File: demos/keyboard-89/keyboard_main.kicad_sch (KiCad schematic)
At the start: 7 parts, among them J2 SWD, U1 RP2040, Y1 12MHz

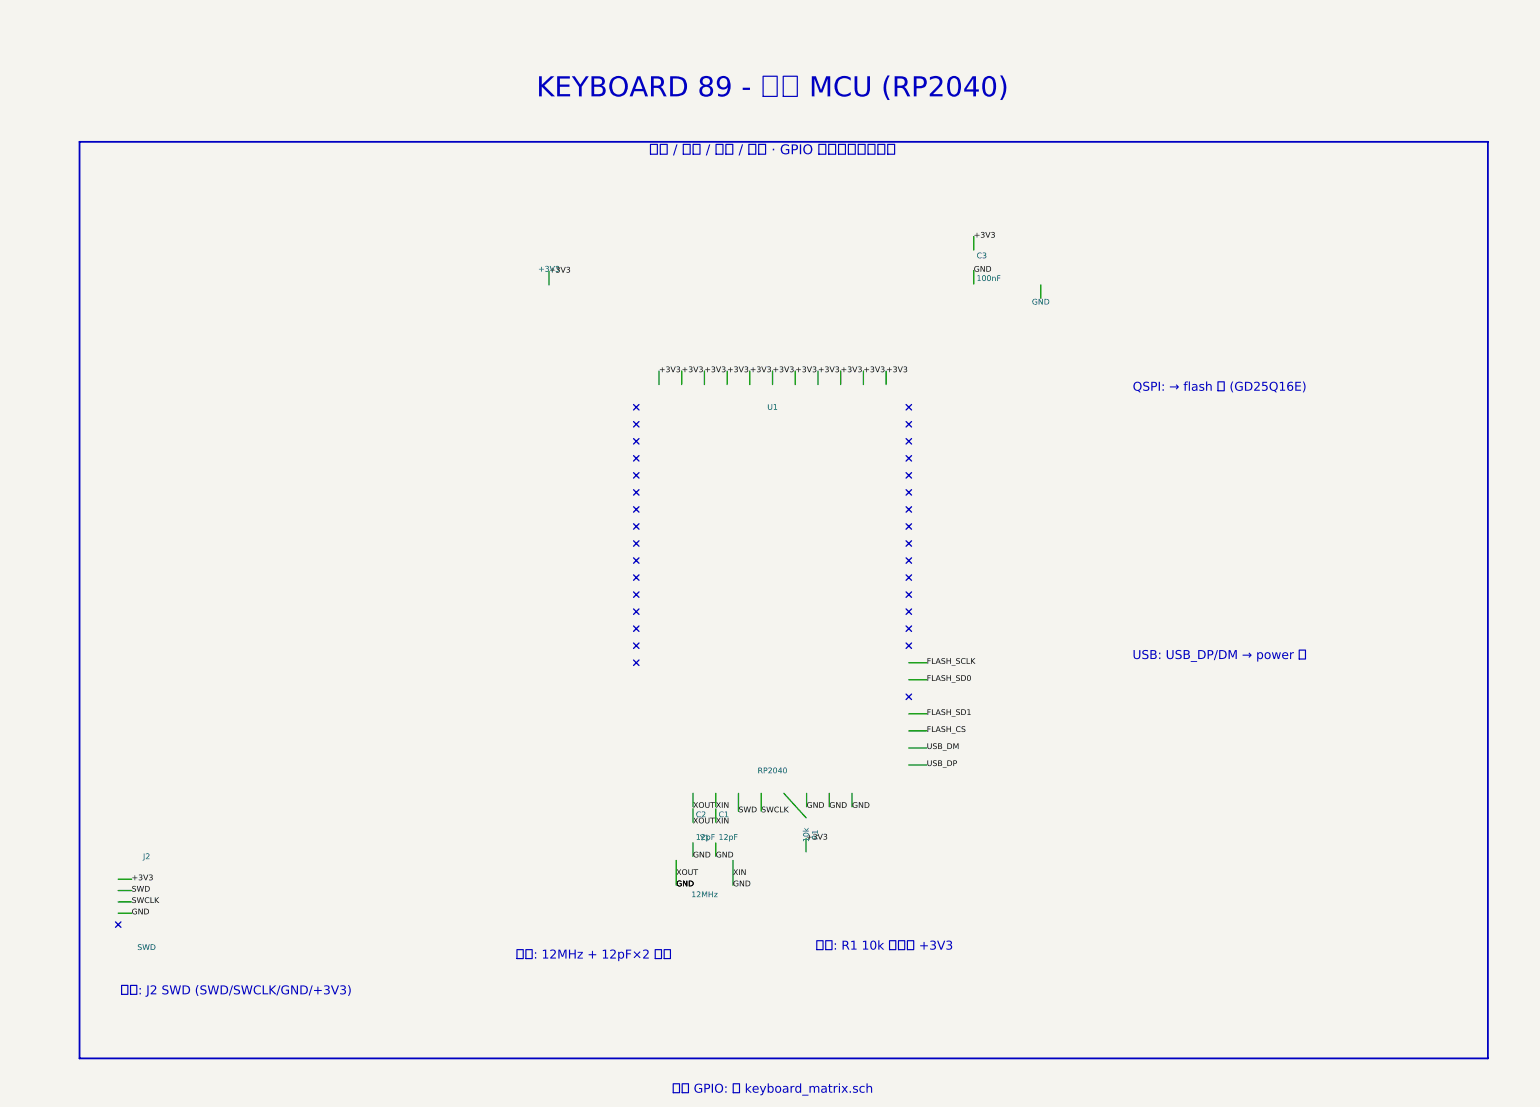
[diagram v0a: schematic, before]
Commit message: fix: update default label height in kicad_sch_add_label function to 1.27mm
feat: add redraw_kb89.py script for redrawing keyboard-89 schematic with new tools
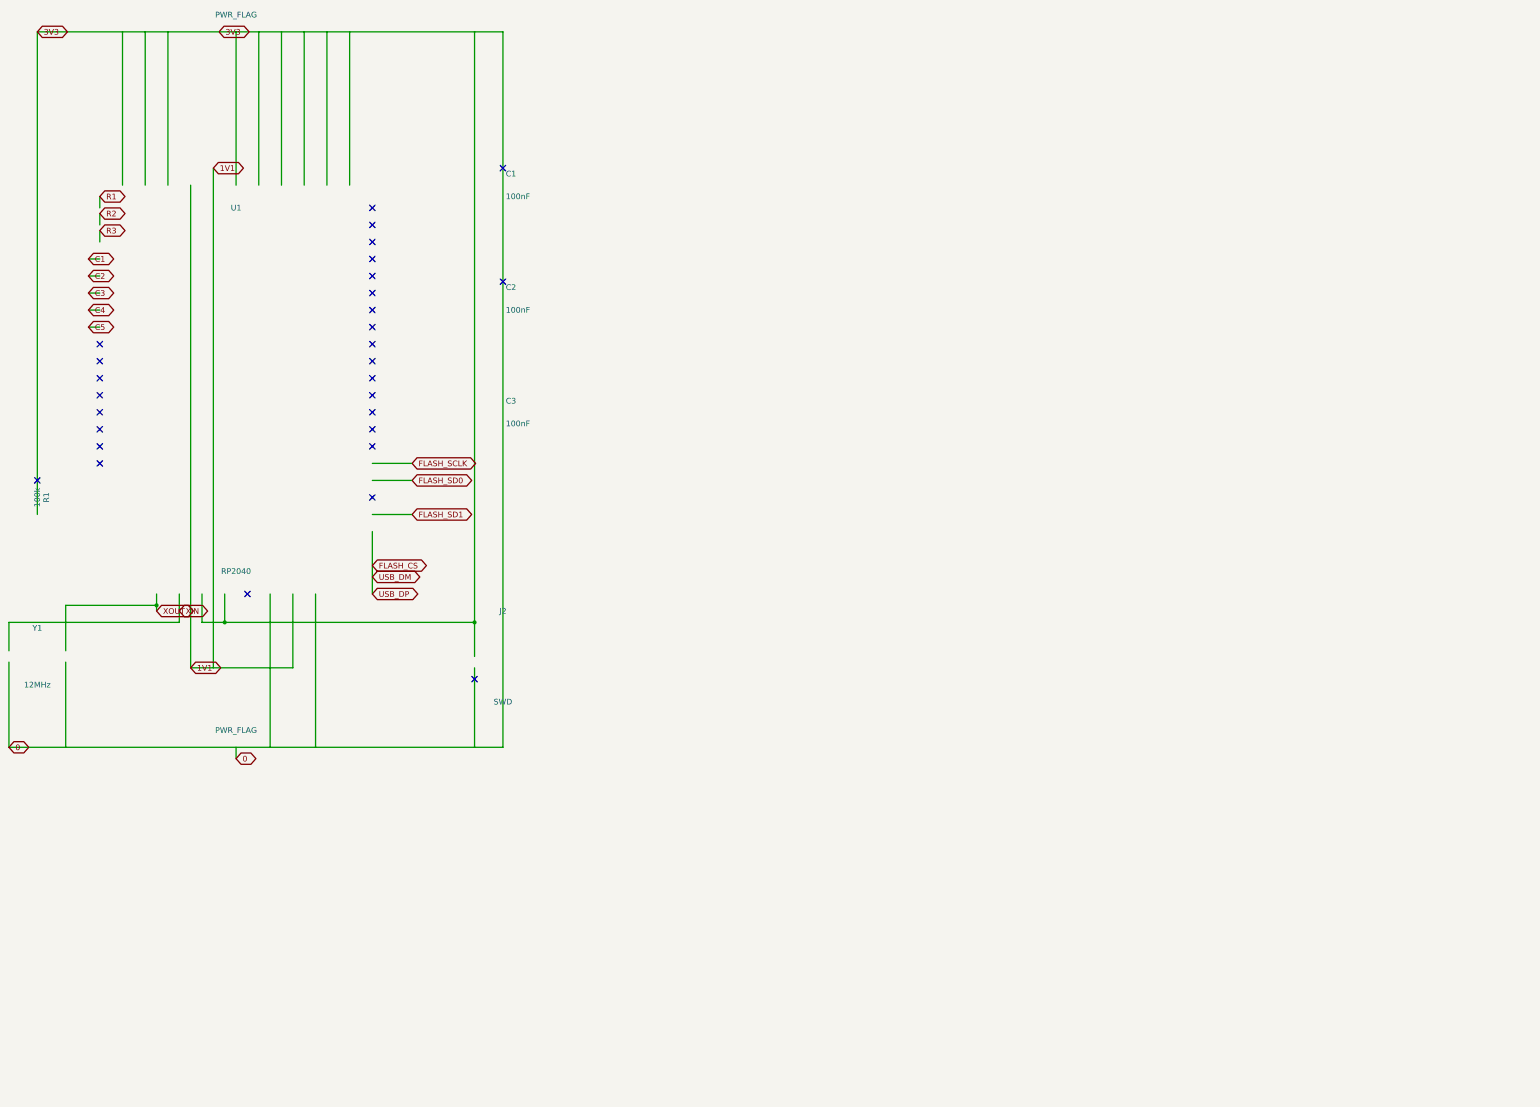
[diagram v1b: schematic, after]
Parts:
- C1, C2: value 12pF -> 100nF
- R1: value 10k -> 100k
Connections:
- net USB_DP is gone; now on net FLASH_CS: U1.47 (USB_DP)
- net at R1.1: no longer U1.26 (RUN)
- net 0: now reaches Y1.4 (GND)
- net 0: now also R1.2
- net R1: now reaches U1.2 (GPIO0)
- net R2: now reaches U1.3 (GPIO1)
- net R3: now reaches U1.4 (GPIO2)
- net C1: now reaches U1.5 (GPIO3)
- net C2: now reaches U1.6 (GPIO4)
- net C3: now reaches U1.7 (GPIO5)
- net C4: now reaches U1.8 (GPIO6)
- net C5: now reaches U1.9 (GPIO7)
- removed net +3V3: C3.1, J2.1, R1.2, U1.1 (IOVDD), U1.10 (IOVDD), U1.22 (IOVDD), U1.23 (DVDD), U1.33 (IOVDD), U1.42 (IOVDD), U1.43 (ADC_AVDD), U1.44 (VREG_VIN), U1.48 (USB_VDD), U1.49 (IOVDD), U1.50 (DVDD)
- removed net GND: C1.1, C1.2, C2.1, C2.2, C3.2, J2.4, U1.19 (TESTEN), U1.20 (XIN), U1.21 (XOUT), U1.45 (VREG_VOUT), U1.57 (GND), Y1.1 (OSC1), Y1.3 (OSC2)
- net SWCLK: no longer names the net of J2.3, U1.24 (SWCLK)
- net SWCLK: now also U1.25 (SWD)
- net SWD: no longer names the net of J2.2
- net SWD: no longer U1.25 (SWD)
- net USB_DM: no longer names the net of U1.46 (USB_DM)
- new net 1V1: U1.45 (VREG_VOUT), U1.50 (DVDD)
- new net XIN: U1.20 (XIN), Y1.1 (OSC1)
- new net XOUT: U1.21 (XOUT), Y1.3 (OSC2)
- no-connect marks 33 -> 29
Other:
- note removed: "KEYBOARD 89 - 主控 MCU (RP2040)"
- note removed: "QSPI: → flash 页 (GD25Q16E)"
- note removed: "USB: USB_DP/DM → power 页"
- note removed: "复位: R1 10k 上拉至 +3V3"
- note removed: "时钟 / 电源 / 复位 / 调试 · GPIO 与矩阵连接见各页"
- note removed: "时钟: 12MHz + 12pF×2 负载"
- note removed: "矩阵 GPIO: 见 keyboard_matrix.sch"
- note removed: "调试: J2 SWD (SWD/SWCLK/GND/+3V3)"

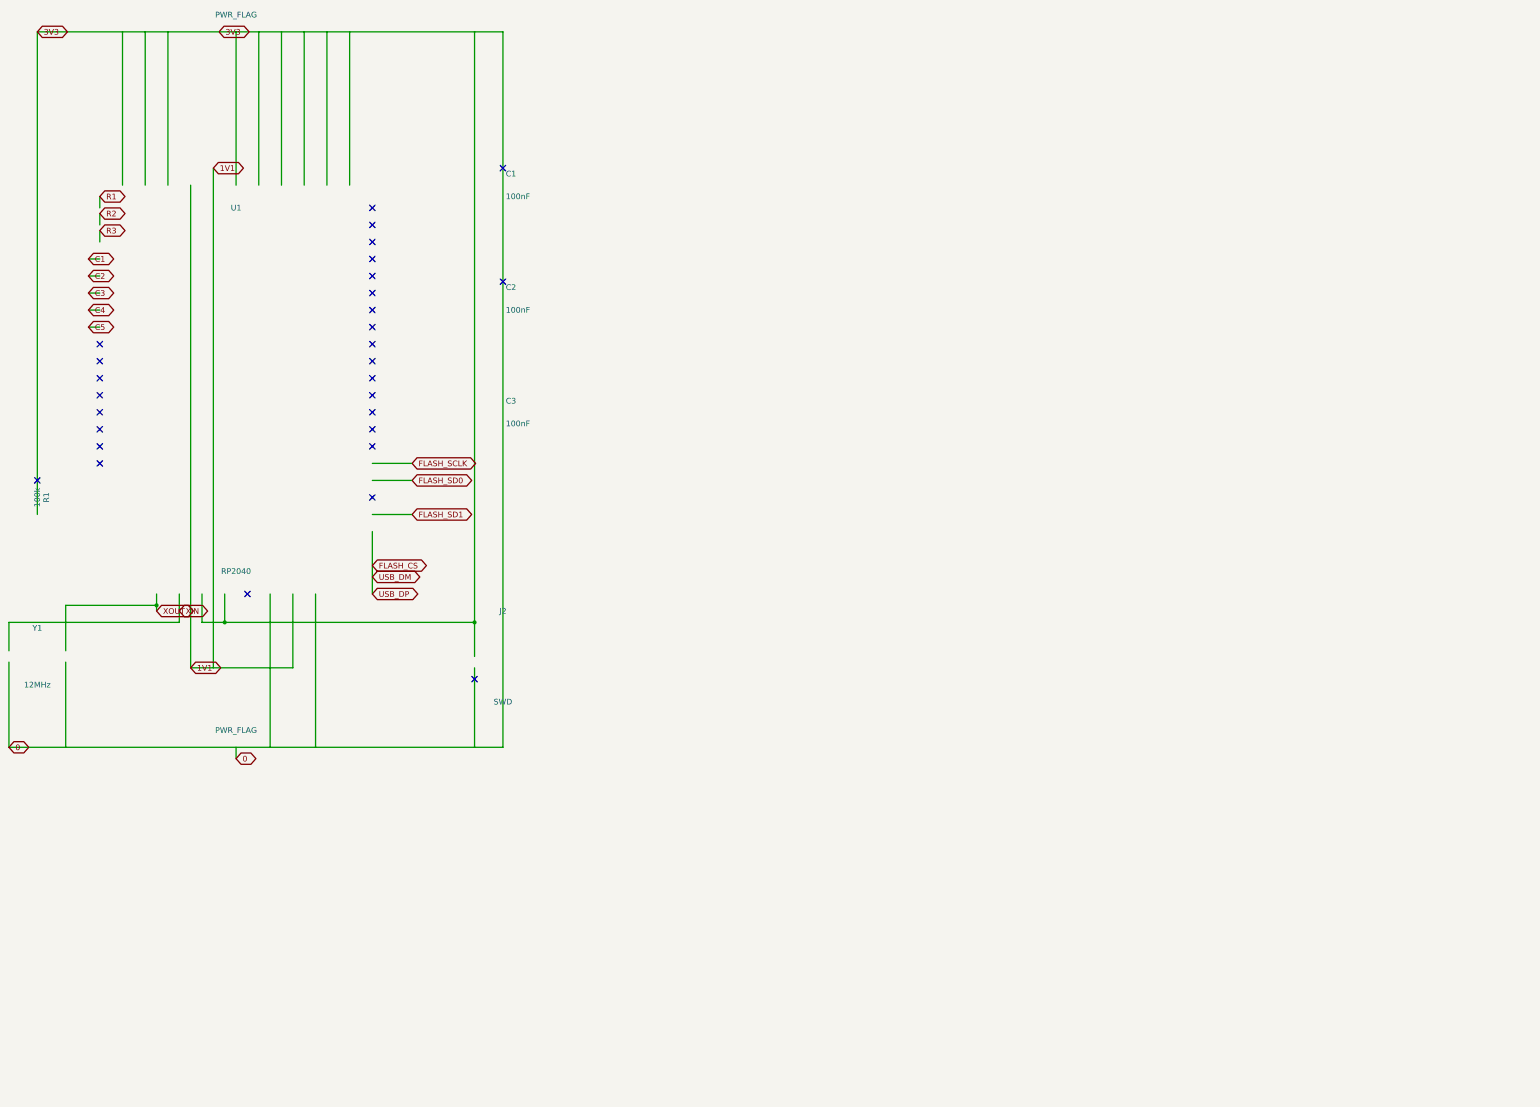
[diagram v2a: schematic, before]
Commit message: Add ERC report, AI setup documentation, and bootstrap scripts
- Created a new ERC report for the keyboard-89 project detailing isolated pin labels and library issues.
- Added AI environment bootstrap documentation for setting up the development environment on Windows and Linux.
- Implemented a PowerShell bootstrap script for Windows to automate the setup of dependencies, environment, and build process.
- Developed a corresponding bash bootstrap script for Linux with similar functionality.
- Introduced a new test for verifying pin connections in the symbol writer module.
- Added JSON report for failed drawing processes with a specific error message in Chinese.
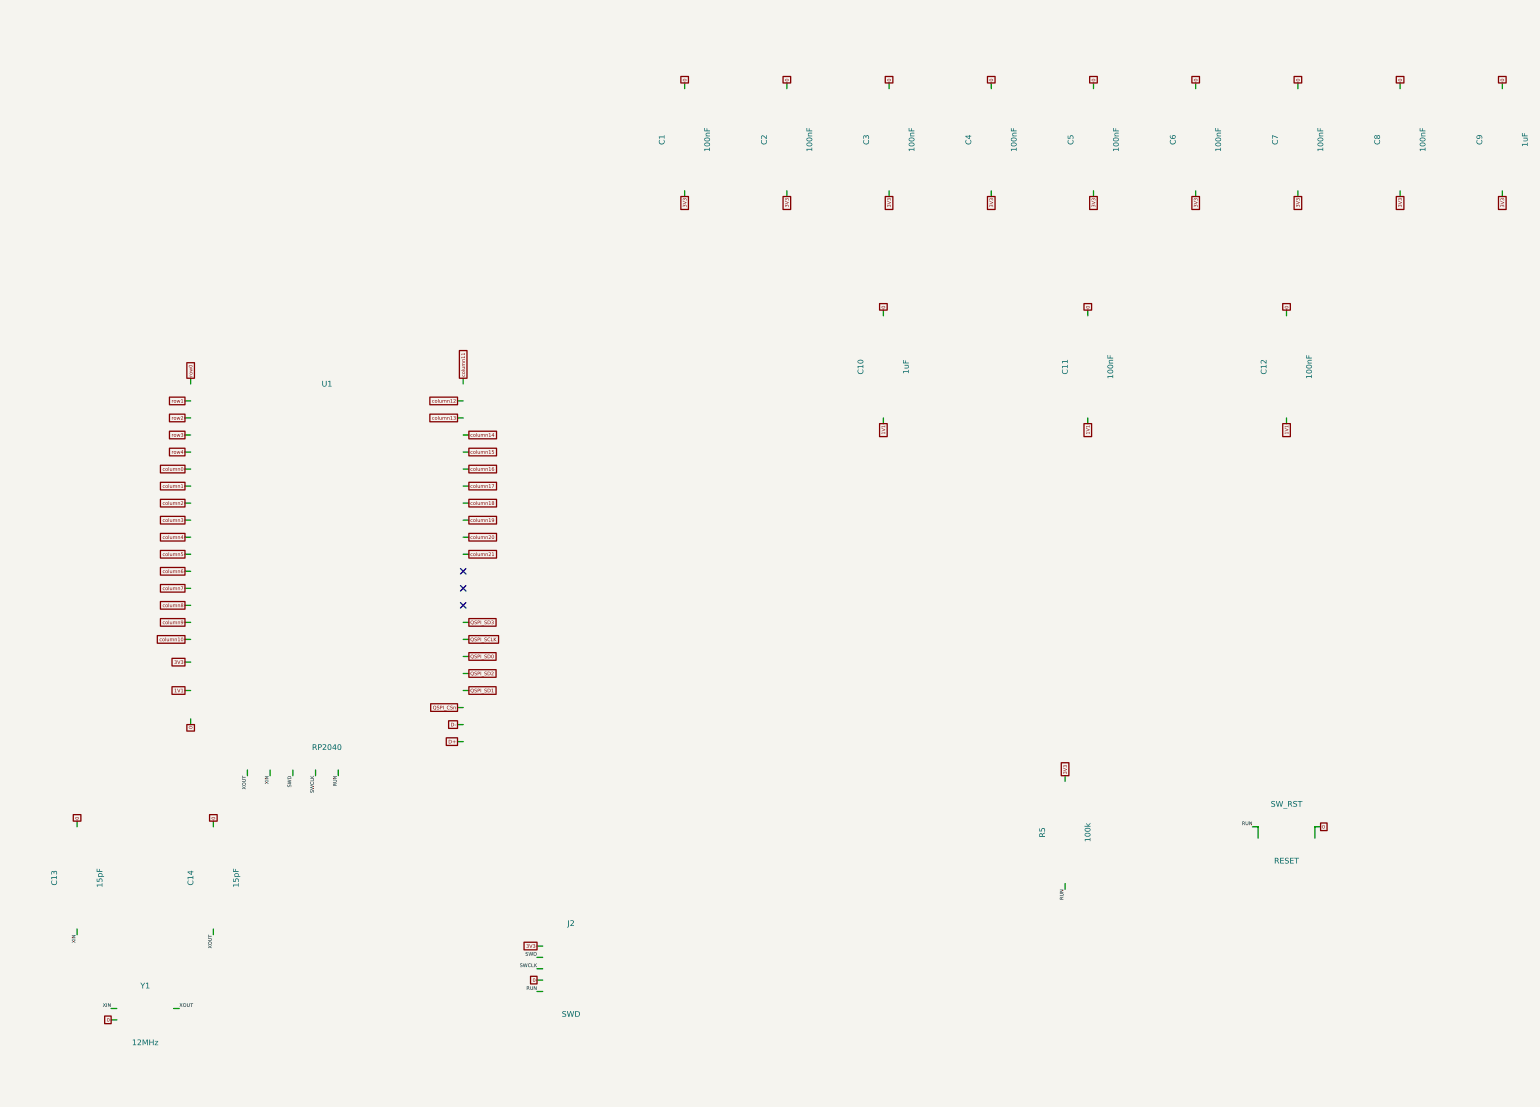
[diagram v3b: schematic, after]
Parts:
- removed C1, C2, C3: 100nF, symbol Device:C
- removed R1: 100k, symbol Device:R
- added C1, C11, C12, C2, C3, C4, C5, C6, C7, C8: 100nF, keyboard-89_local:C_0402_1005Metric, symbol keyboard-89_local:C_GENERIC
- added C10, C9: 1uF, keyboard-89_local:C_0402_1005Metric, symbol keyboard-89_local:C_GENERIC
- added C13, C14: 15pF, keyboard-89_local:C_0402_1005Metric, symbol keyboard-89_local:C_GENERIC
- added R5: 100k, keyboard-89_local:R_0402_1005Metric, symbol keyboard-89_local:R_GENERIC
- added SW_RST: RESET, keyboard-89_local:TC-6601-5-160G, symbol keyboard-89_local:TC-6601-5-160G
- J2: footprint Connector_PinHeader:PinHeader_1x05_P2.54mm_Vertical -> keyboard-89_local:PinHeader_1x05_P2.54mm_Vertical
- U1: footprint Package_DFN_QFN:QFN-56-1EP_7x7mm_P0.4mm_EP3.2x3.2mm -> keyboard-89_local:QFN-56-1EP_7x7mm_P0.4mm_EP3.2x3.2mm
- Y1: footprint Crystal_SMD:3215_4Pin_3.2x1.5mm -> keyboard-89_local:Crystal_YSX321SL
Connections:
- net 0: now also J2.4, U1.19 (TESTEN), U1.57 (GND), Y1.2 (GND), C1.2, C10.2, C11.2, C12.2, C13.2, C14.2, C2.2, C3.2, C4.2, C5.2, C6.2, C7.2, C8.2, C9.2, SW_RST.3, SW_RST.4
- net 1V1: now also U1.23 (DVDD), C10.1, C11.1, C12.1
- net XIN: now also C13.1
- net XOUT: now also C14.1
- net 3V3: now reaches U1.1 (IOVDD)
- net 3V3: now also J2.1, U1.10 (IOVDD), U1.22 (IOVDD), U1.33 (IOVDD), U1.42 (IOVDD), U1.43 (ADC_AVDD), U1.44 (VREG_VIN), U1.48 (USB_VDD), U1.49 (IOVDD), C1.1, C2.1, C3.1, C4.1, C5.1, C6.1, C7.1, C8.1, C9.1, R5.2
- net column3: now reaches U1.11 (GPIO8)
- net column4: now reaches U1.12 (GPIO9)
- net column5: now reaches U1.13 (GPIO10)
- net column6: now reaches U1.14 (GPIO11)
- net column7: now reaches U1.15 (GPIO12)
- net column8: now reaches U1.16 (GPIO13)
- net column9: now reaches U1.17 (GPIO14)
- net column10: now reaches U1.18 (GPIO15)
- net SWCLK: now reaches J2.3, U1.24 (SWCLK)
- net SWCLK: no longer U1.25 (SWD)
- net RUN: now reaches U1.26 (RUN)
- net RUN: now also J2.5, R5.1, SW_RST.1, SW_RST.2
- net column11: now reaches U1.27 (GPIO16)
- net column12: now reaches U1.28 (GPIO17)
- net column13: now reaches U1.29 (GPIO18)
- net column14: now reaches U1.30 (GPIO19)
- net column15: now reaches U1.31 (GPIO20)
- net column16: now reaches U1.32 (GPIO21)
- net column17: now reaches U1.34 (GPIO22)
- net column18: now reaches U1.35 (GPIO23)
- net column19: now reaches U1.36 (GPIO24)
- net column20: now reaches U1.37 (GPIO25)
- net column21: now reaches U1.38 (GPIO26)
- net D-: now reaches U1.46 (USB_DM)
- net QSPI_SD3: now reaches U1.51 (QSPI_SD3)
- net QSPI_SD2: now reaches U1.54 (QSPI_SD2)
- net SWD: now reaches J2.2
- net SWD: now also U1.25 (SWD)
- net C1 renamed row3
- net C2 renamed row4
- net C3 renamed column0
- net C4 renamed column1
- net C5 renamed column2
- net FLASH_CS renamed D+
- net D+: no longer U1.56 (QSPI_CSn)
- net FLASH_SCLK renamed QSPI_SCLK
- net FLASH_SD0 renamed QSPI_SD0
- net FLASH_SD1 renamed QSPI_SD1
- net R1 renamed row0
- net R2 renamed row1
- net R3 renamed row2
- new net QSPI_CSn: U1.56 (QSPI_CSn)
- no-connect marks 29 -> 3
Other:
- company: (none) -> Keyboard-89
- title: keyboard_main -> Keyboard-89 RP2040 Core
